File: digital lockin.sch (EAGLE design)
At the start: 24 parts, among them IC1 OPA2650E, IC2 LM358D, T2 NPN, U2 RASPBERRY_PICOSMD-TH, U5 TL431AIDBZR

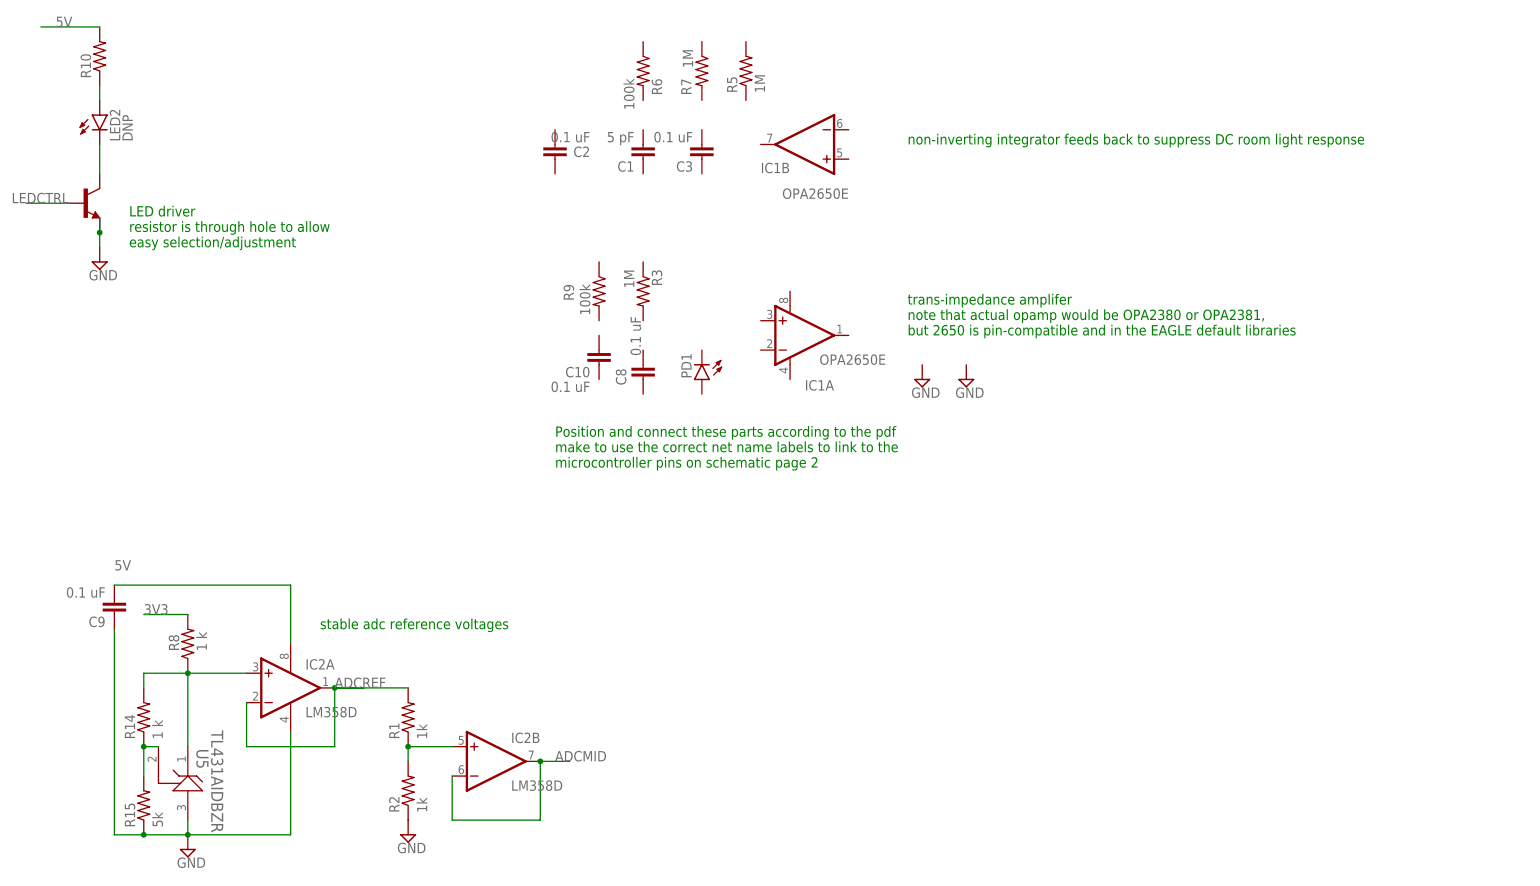
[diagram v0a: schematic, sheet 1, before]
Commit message: Lab 3 lock-in amplifier
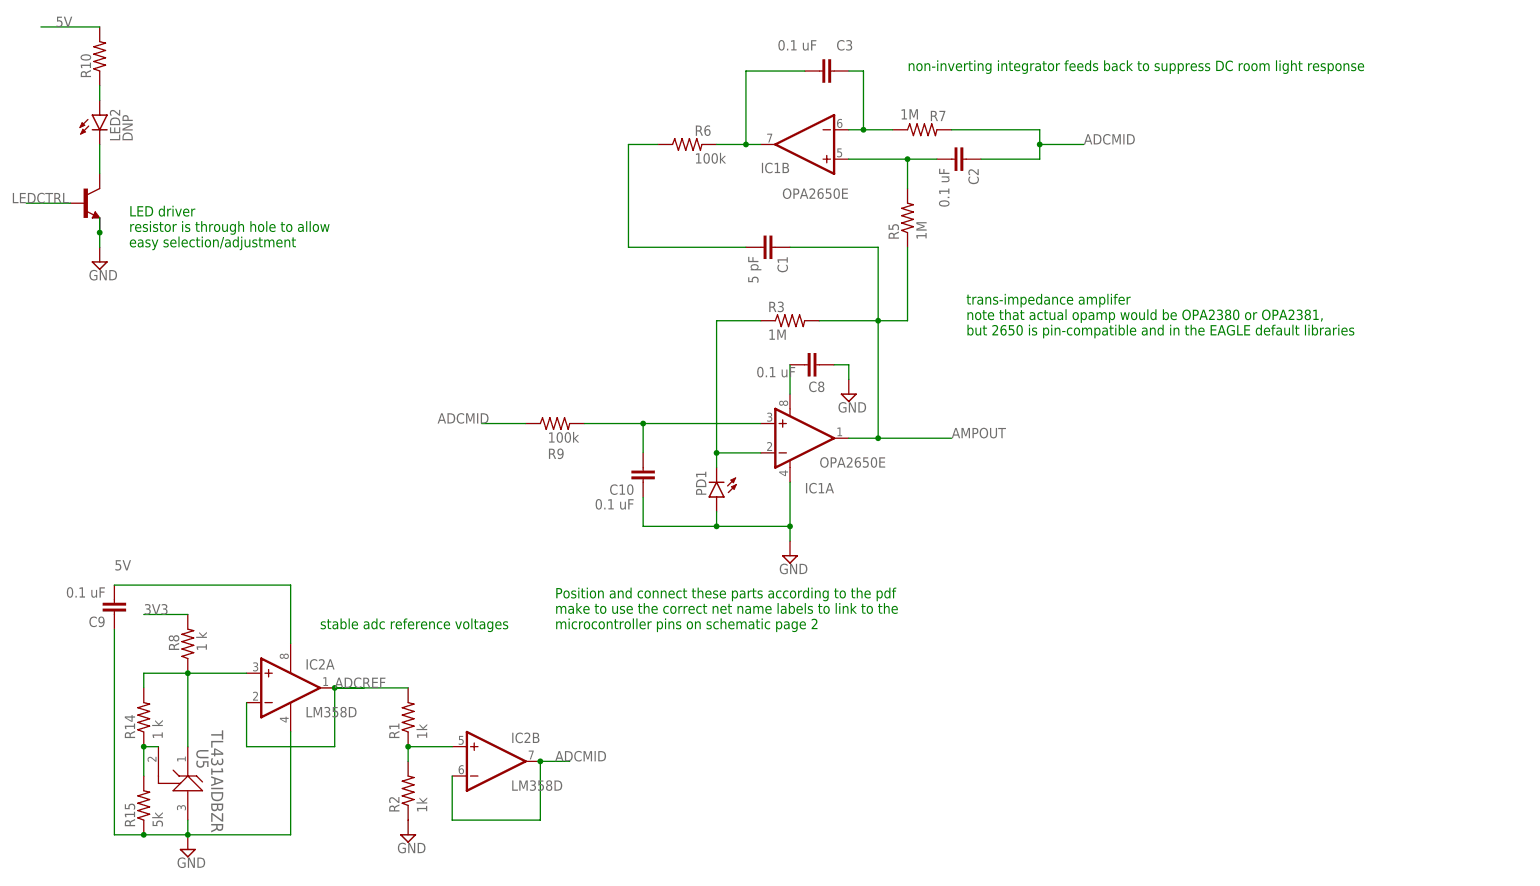
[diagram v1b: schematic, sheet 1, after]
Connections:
- new net N$1: C3.2, IC1B.OUT, R6.2
- new net N$13: C10.2, IC1A.+IN, R9.2
- new net N$2: C3.1, IC1B.-IN, R7.1
- new net N$4: C2.2, IC1B.+IN, R5.2
- new net N$6: C1.2, R6.1
- new net N$7: IC1A.-IN, PD1.C, R3.1
- new net N$8: C8.2, IC1A.V+
- net ADCMID: now also C2.1, R7.2, R9.1
- net AMPOUT: now also C1.1, IC1A.OUT, R3.2, R5.1
- net GND: now also C10.1, C8.1, IC1A.V-, PD1.A
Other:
- moved on the sheet: C1, C10, C2, C3, C8, IC1A, PD1, R3, R5, R6, R7, R9
